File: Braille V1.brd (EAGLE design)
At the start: 98 x 89.6 mm, 85 parts, among them IC1 TD62083, IC2 74HC238D, IC3 74HC238D, IC4 TD62083, IC5 74HC238D, IC6 74HC238D, J1 POWER_JACKSLT, Q1 TBD62783AFG,EL, Q2 TBD62783AFG,EL, U2 LM317

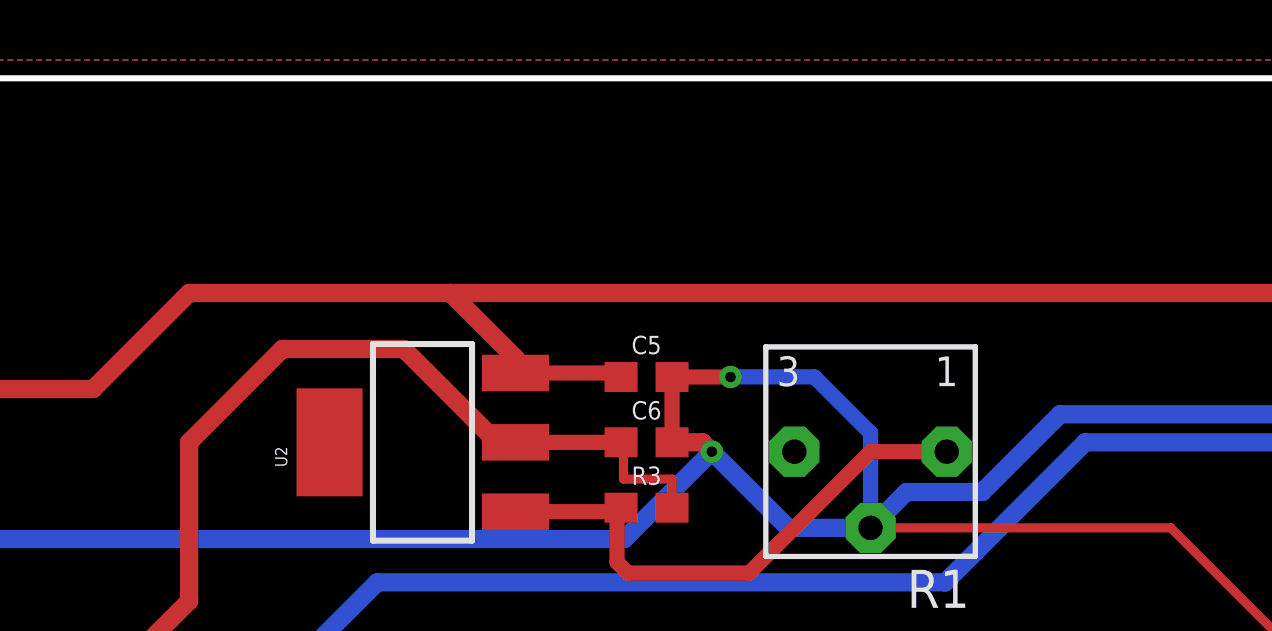
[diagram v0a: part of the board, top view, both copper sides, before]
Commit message: Updated Test Point
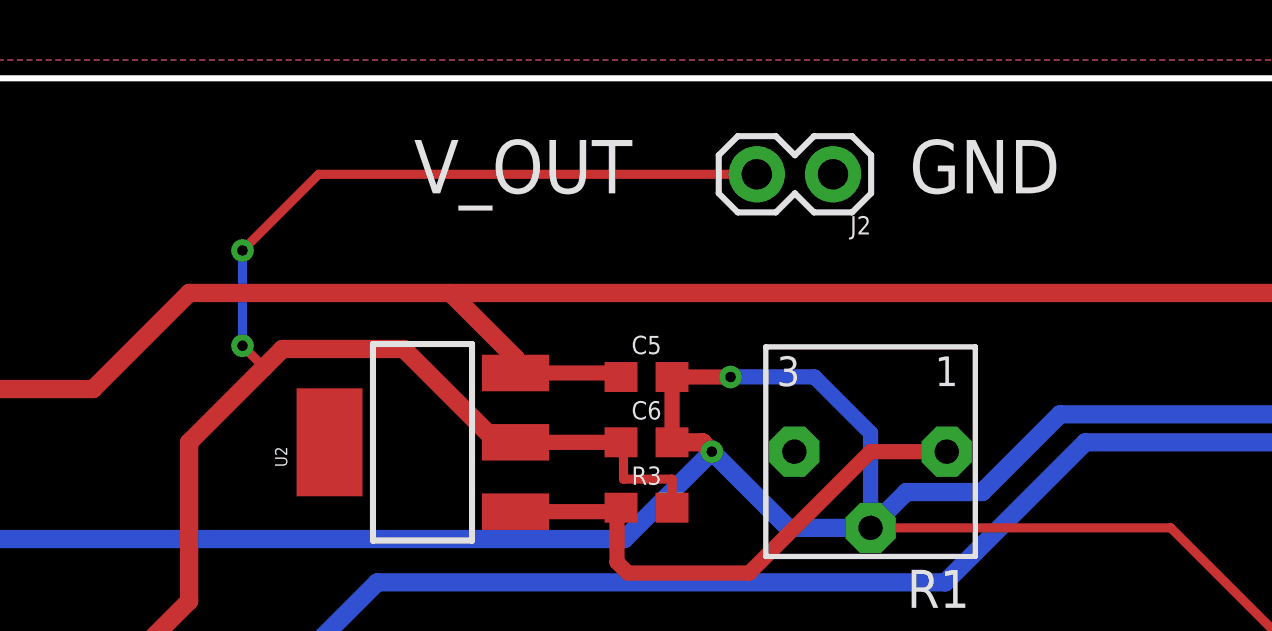
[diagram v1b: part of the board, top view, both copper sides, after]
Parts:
- added J2: (no value), SparkFun-Connectors:1X02
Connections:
- net 12V: now also J2.2
- net GND: now also J2.1
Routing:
- net 12V: track 112.5 -> 134.8 mm, vias 0 -> 2
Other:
- board text added: "GND"
- board text added: "V_OUT"
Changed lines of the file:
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@@
 <text x="9.525" y="66.04" size="1.016" layer="25">Jump to power from Arduino</text>
 <text x="96.52" y="50.8" size="1.778" layer="25" rot="R90">@vjvarada</text>
+<text x="32.385" y="88.265" size="1.778" layer="25">V_OUT</text>
+<text x="48.895" y="88.265" size="1.778" layer="25">GND</text>
 </plain>
 <attributes>
@@
 </element>
 <element name="LOGO1" library="SparkFun-Aesthetics" package="OSHW-LOGO-L_COPPER" value="OSHW-LOGOL-COPPER" x="99.06" y="15.24" smashed="yes" rot="R90"/>
+<element name="J2" library="SparkFun-Connectors" package="1X02" value="" x="46.355" y="88.9" smashed="yes" rot="R180">
+<attribute name="NAME" x="47.625" y="87.503" size="0.6096" layer="25" font="vector" ratio="20" rot="R180"/>
+<attribute name="VALUE" x="47.625" y="90.932" size="0.6096" layer="27" font="vector" ratio="20" rot="R180"/>
+</element>
 </elements>
 <signals>
@@
 <vertex x="6.35" y="1.905"/>
 </polygon>
+<contactref element="J2" pad="1"/>
 </signal>
 <signal name="N$1">
@@
 <wire x1="35.15995" y1="79.96555" x2="32.04845" y2="83.07705" width="0.6096" layer="1"/>
 <wire x1="32.04845" y1="83.07705" x2="28.0035" y2="83.07705" width="0.6096" layer="1"/>
-<wire x1="28.0035" y1="83.07705" x2="24.892" y2="79.96555" width="0.6096" layer="1"/>
+<wire x1="28.0035" y1="83.07705" x2="27.390725" y2="82.464275" width="0.6096" layer="1"/>
+<wire x1="27.390725" y1="82.464275" x2="24.892" y2="79.96555" width="0.6096" layer="1"/>
 <wire x1="24.892" y1="79.96555" x2="24.892" y2="74.676" width="0.6096" layer="1"/>
 <wire x1="24.892" y1="74.676" x2="22.09165" y2="71.87565" width="0.6096" layer="1"/>
@@
 <wire x1="39.37" y1="79.96555" x2="39.37" y2="78.74" width="0.3048" layer="1"/>
 <wire x1="39.37" y1="78.74" x2="40.98835" y2="78.74" width="0.3048" layer="1"/>
+<contactref element="J2" pad="2"/>
+<wire x1="43.815" y1="88.9" x2="29.21" y2="88.9" width="0.3048" layer="1"/>
+<wire x1="29.21" y1="88.9" x2="26.67" y2="86.36" width="0.3048" layer="1"/>
+<via x="26.67" y="86.36" extent="1-16" drill="0.35"/>
+<wire x1="26.67" y1="86.36" x2="26.67" y2="83.185" width="0.3048" layer="16"/>
+<via x="26.67" y="83.185" extent="1-16" drill="0.35"/>
+<wire x1="26.67" y1="83.185" x2="27.390725" y2="82.464275" width="0.3048" layer="1"/>
 </signal>
 <signal name="N$32">
